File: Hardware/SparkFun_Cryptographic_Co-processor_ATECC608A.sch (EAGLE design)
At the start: 22 parts, among them J1 QWIIC, J2 QWIIC, J3 PTH, U1 ATECC608A

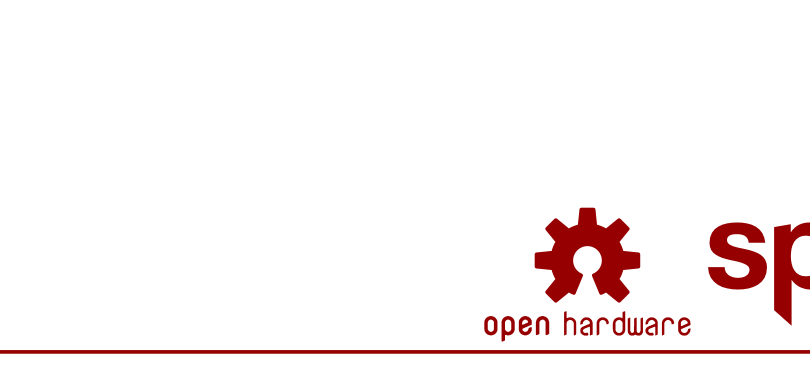
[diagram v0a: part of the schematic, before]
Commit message: eng 1st run checklist stuff
-added qwiic logo as device so it has logo in SCH
-update vector font to "non-legacy"
-cleaned up assembly sheet view attribute placement
-IC datasheet (summary only)
-measures updated, PNG and PDF files created.
-Exported SCH as PDF in docs
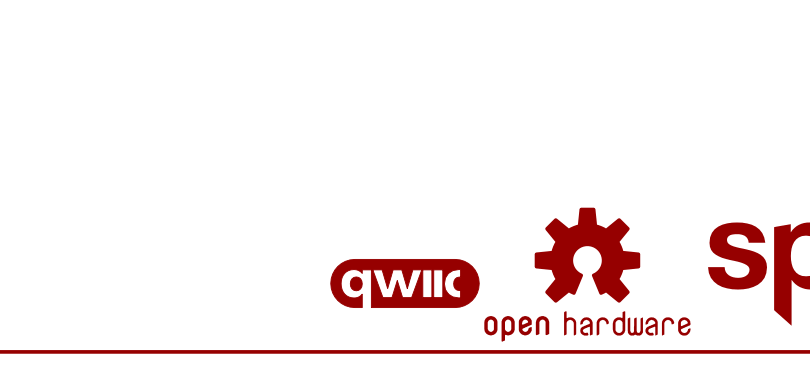
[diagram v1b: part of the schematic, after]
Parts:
- added LOGO3: QWIIC_LOGO_4MM, SparkFun-Aesthetics:QWIIC_LOGO_4MM
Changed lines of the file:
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@@
 <settings>
 <setting alwaysvectorfont="no"/>
-<setting keepoldvectorfont="yes"/>
 <setting verticaltext="up"/>
 </settings>
@@
 <part name="H3" library="SparkFun-Hardware" deviceset="STAND-OFF" device=""/>
 <part name="U1" library="SparkFun-IC-Special-Function" deviceset="ATECC608A" device="UDFN_2X3MM" value="ATECC608A"/>
+<part name="LOGO3" library="SparkFun-Aesthetics" deviceset="QWIIC_LOGO" device="_4MM"/>
 </parts>
 <sheets>
@@
 <attribute name="VALUE" x="114.3" y="121.92" size="1.778" layer="96" font="vector"/>
 </instance>
+<instance part="LOGO3" gate="G$1" x="55.88" y="7.62" smashed="yes"/>
 </instances>
 <busses>

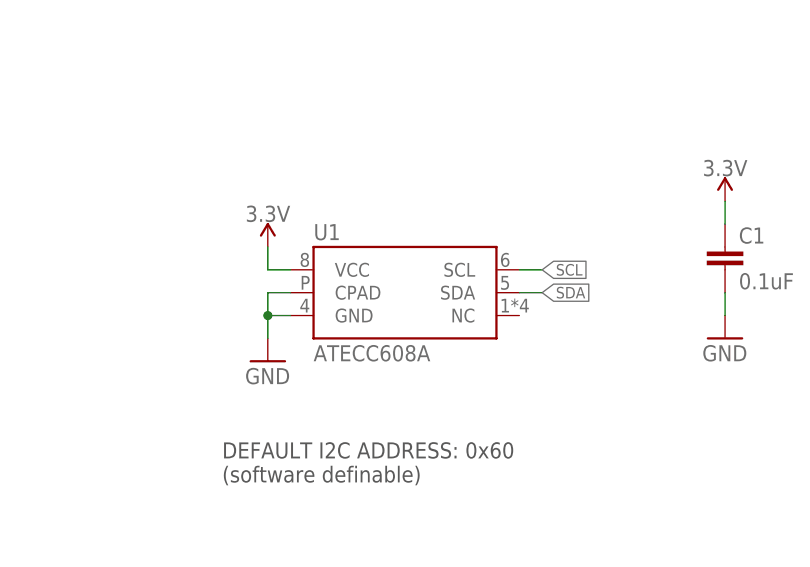
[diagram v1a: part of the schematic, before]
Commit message: Move to dual-type package (UDFN and SOIC)
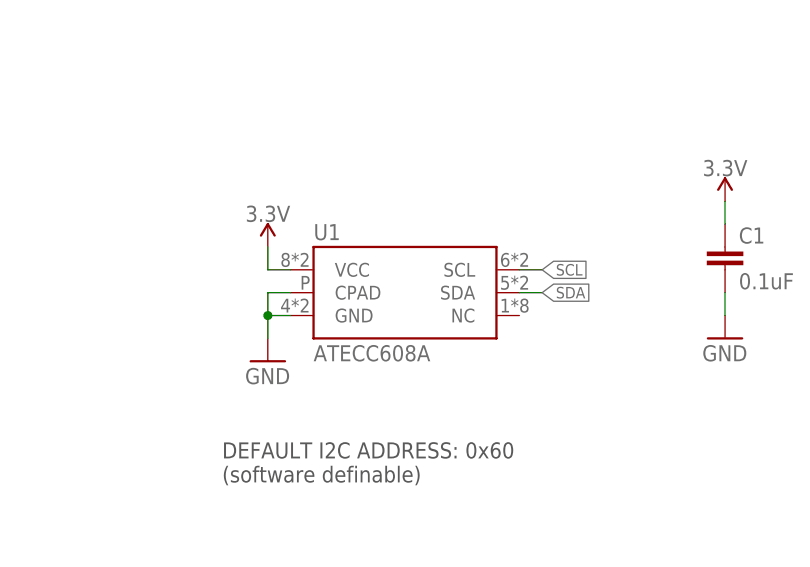
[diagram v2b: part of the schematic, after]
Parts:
- U1: device SparkFun-IC-Special-Function:ATECC608AUDFN_2X3MM -> SparkFun-IC-Special-Function:ATECC608ADUAL_PACKAGE_UDFN_SOIC-8
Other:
- moved on the sheet: U1
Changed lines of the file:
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@@
 <grid distance="0.1" unitdist="inch" unit="inch" style="lines" multiple="1" display="no" altdistance="0.01" altunitdist="inch" altunit="inch"/>
 <layers>
-<layer number="1" name="Top" color="4" fill="1" visible="no" active="no"/>
-<layer number="2" name="Route2" color="1" fill="3" visible="no" active="no"/>
-<layer number="3" name="Route3" color="4" fill="3" visible="no" active="no"/>
-<layer number="4" name="Route4" color="1" fill="4" visible="no" active="no"/>
-<layer number="5" name="Route5" color="4" fill="4" visible="no" active="no"/>
-<layer number="6" name="Route6" color="1" fill="8" visible="no" active="no"/>
-<layer number="7" name="Route7" color="4" fill="8" visible="no" active="no"/>
-<layer number="8" name="Route8" color="1" fill="2" visible="no" active="no"/>
-<layer number="9" name="Route9" color="4" fill="2" visible="no" active="no"/>
-<layer number="10" name="Route10" color="1" fill="7" visible="no" active="no"/>
-<layer number="11" name="Route11" color="4" fill="7" visible="no" active="no"/>
-<layer number="12" name="Route12" color="1" fill="5" visible="no" active="no"/>
-<layer number="13" name="Route13" color="4" fill="5" visible="no" active="no"/>
-<layer number="14" name="Route14" color="1" fill="6" visible="no" active="no"/>
-<layer number="15" name="Route15" color="4" fill="6" visible="no" active="no"/>
-<layer number="16" name="Bottom" color="1" fill="1" visible="no" active="no"/>
-<layer number="17" name="Pads" color="2" fill="1" visible="no" active="no"/>
-<layer number="18" name="Vias" color="2" fill="1" visible="no" active="no"/>
-<layer number="19" name="Unrouted" color="6" fill="1" visible="no" active="no"/>
-<layer number="20" name="Dimension" color="24" fill="1" visible="no" active="no"/>
-<layer number="21" name="tPlace" color="16" fill="1" visible="no" active="no"/>
-<layer number="22" name="bPlace" color="14" fill="1" visible="no" active="no"/>
-<layer number="23" name="tOrigins" color="15" fill="1" visible="no" active="no"/>
-<layer number="24" name="bOrigins" color="15" fill="1" visible="no" active="no"/>
-<layer number="25" name="tNames" color="7" fill="1" visible="no" active="no"/>
-<layer number="26" name="bNames" color="7" fill="1" visible="no" active="no"/>
-<layer number="27" name="tValues" color="7" fill="1" visible="no" active="no"/>
-<layer number="28" name="bValues" color="7" fill="1" visible="no" active="no"/>
+<layer number="1" name="Top" color="4" fill="1" visible="yes" active="no"/>
+<layer number="2" name="Route2" color="1" fill="3" visible="yes" active="no"/>
+<layer number="3" name="Route3" color="4" fill="3" visible="yes" active="no"/>
+<layer number="4" name="Route4" color="1" fill="4" visible="yes" active="no"/>
+<layer number="5" name="Route5" color="4" fill="4" visible="yes" active="no"/>
+<layer number="6" name="Route6" color="1" fill="8" visible="yes" active="no"/>
+<layer number="7" name="Route7" color="4" fill="8" visible="yes" active="no"/>
+<layer number="8" name="Route8" color="1" fill="2" visible="yes" active="no"/>
+<layer number="9" name="Route9" color="4" fill="2" visible="yes" active="no"/>
+<layer number="10" name="Route10" color="1" fill="7" visible="yes" active="no"/>
+<layer number="11" name="Route11" color="4" fill="7" visible="yes" active="no"/>
+<layer number="12" name="Route12" color="1" fill="5" visible="yes" active="no"/>
+<layer number="13" name="Route13" color="4" fill="5" visible="yes" active="no"/>
+<layer number="14" name="Route14" color="1" fill="6" visible="yes" active="no"/>
+<layer number="15" name="Route15" color="4" fill="6" visible="yes" active="no"/>
+<layer number="16" name="Bottom" color="1" fill="1" visible="yes" active="no"/>
+<layer number="17" name="Pads" color="2" fill="1" visible="yes" active="no"/>
+<layer number="18" name="Vias" color="2" fill="1" visible="yes" active="no"/>
+<layer number="19" name="Unrouted" color="6" fill="1" visible="yes" active="no"/>
+<layer number="20" name="Dimension" color="24" fill="1" visible="yes" active="no"/>
+<layer number="21" name="tPlace" color="16" fill="1" visible="yes" active="no"/>
+<layer number="22" name="bPlace" color="14" fill="1" visible="yes" active="no"/>
+<layer number="23" name="tOrigins" color="15" fill="1" visible="yes" active="no"/>
+<layer number="24" name="bOrigins" color="15" fill="1" visible="yes" active="no"/>
+<layer number="25" name="tNames" color="7" fill="1" visible="yes" active="no"/>
+<layer number="26" name="bNames" color="7" fill="1" visible="yes" active="no"/>
+<layer number="27" name="tValues" color="7" fill="1" visible="yes" active="no"/>
+<layer number="28" name="bValues" color="7" fill="1" visible="yes" active="no"/>
 <layer number="29" name="tStop" color="7" fill="3" visible="no" active="no"/>
 <layer number="30" name="bStop" color="7" fill="6" visible="no" active="no"/>
@@
 <layer number="35" name="tGlue" color="7" fill="4" visible="no" active="no"/>
 <layer number="36" name="bGlue" color="7" fill="5" visible="no" active="no"/>
-<layer number="37" name="tTest" color="7" fill="1" visible="no" active="no"/>
-<layer number="38" name="bTest" color="7" fill="1" visible="no" active="no"/>
+<layer number="37" name="tTest" color="7" fill="1" visible="yes" active="no"/>
+<layer number="38" name="bTest" color="7" fill="1" visible="yes" active="no"/>
 <layer number="39" name="tKeepout" color="4" fill="11" visible="no" active="no"/>
 <layer number="40" name="bKeepout" color="1" fill="11" visible="no" active="no"/>
@@
 <layer number="44" name="Drills" color="7" fill="1" visible="no" active="no"/>
 <layer number="45" name="Holes" color="7" fill="1" visible="no" active="no"/>
-<layer number="46" name="Milling" color="3" fill="1" visible="no" active="no"/>
-<layer number="47" name="Measures" color="7" fill="1" visible="no" active="no"/>
-<layer number="48" name="Document" color="7" fill="1" visible="no" active="no"/>
-<layer number="49" name="Reference" color="13" fill="1" visible="no" active="no"/>
-<layer number="50" name="dxf" color="7" fill="1" visible="no" active="no"/>
-<layer number="51" name="tDocu" color="6" fill="1" visible="no" active="no"/>
-<layer number="52" name="bDocu" color="7" fill="1" visible="no" active="no"/>
-<layer number="53" name="tGND_GNDA" color="7" fill="9" visible="no" active="no"/>
-<layer number="54" name="bGND_GNDA" color="1" fill="9" visible="no" active="no"/>
-<layer number="56" name="wert" color="7" fill="1" visible="no" active="no"/>
-<layer number="57" name="tCAD" color="7" fill="1" visible="no" active="no"/>
-<layer number="59" name="tCarbon" color="7" fill="1" visible="no" active="no"/>
-<layer number="60" name="bCarbon" color="7" fill="1" visible="no" active="no"/>
+<layer number="46" name="Milling" color="3" fill="1" visible="yes" active="no"/>
+<layer number="47" name="Measures" color="7" fill="1" visible="yes" active="no"/>
+<layer number="48" name="Document" color="7" fill="1" visible="yes" active="no"/>
+<layer number="49" name="Reference" color="13" fill="1" visible="yes" active="no"/>
+<layer number="50" name="dxf" color="7" fill="1" visible="yes" active="no"/>
+<layer number="51" name="tDocu" color="6" fill="1" visible="yes" active="no"/>
+<layer number="52" name="bDocu" color="7" fill="1" visible="yes" active="no"/>
+<layer number="53" name="tGND_GNDA" color="7" fill="9" visible="yes" active="no"/>
+<layer number="54" name="bGND_GNDA" color="1" fill="9" visible="yes" active="no"/>
+<layer number="56" name="wert" color="7" fill="1" visible="yes" active="no"/>
+<layer number="57" name="tCAD" color="7" fill="1" visible="yes" active="no"/>
+<layer number="59" name="tCarbon" color="7" fill="1" visible="yes" active="no"/>
+<layer number="60" name="bCarbon" color="7" fill="1" visible="yes" active="no"/>
 <layer number="88" name="SimResults" color="9" fill="1" visible="no" active="yes"/>
 <layer number="89" name="SimProbes" color="9" fill="1" visible="no" active="yes"/>
@@
 <part name="H1" library="SparkFun-Hardware" deviceset="STAND-OFF" device=""/>
 <part name="H3" library="SparkFun-Hardware" deviceset="STAND-OFF" device=""/>
-<part name="U1" library="SparkFun-IC-Special-Function" deviceset="ATECC608A" device="UDFN_2X3MM" value="ATECC608A"/>
+<part name="U1" library="SparkFun-IC-Special-Function" deviceset="ATECC608A" device="DUAL_PACKAGE_UDFN_SOIC-8" value="ATECC608A"/>
 <part name="LOGO3" library="SparkFun-Aesthetics" deviceset="QWIIC_LOGO" device="_4MM"/>
 </parts>
